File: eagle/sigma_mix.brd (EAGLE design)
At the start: 117.5 x 59.5 mm, 155 parts, among them J1 POWER_JACK, J2 RCA_JACK_CUI, J3 RCA_JACK_CUI, J4 RCA_JACK_CUI, J5 RCA_JACK_CUI, J6 RCA_JACK_X2_CUI, J7 RCA_JACK_X2_CUI, J8 RCA_JACK_X2_CUI, J9 RCA_JACK_X2_CUI, U1 MCP1726, U2 MCP73871, U3 ADM811TARTZ-REEL7, U4 ADAU1701JSTZ, U5 ADAU1701JSTZ, X1 2510-, X2 2510-, X3 12.288MHz, X4 12.288MHz

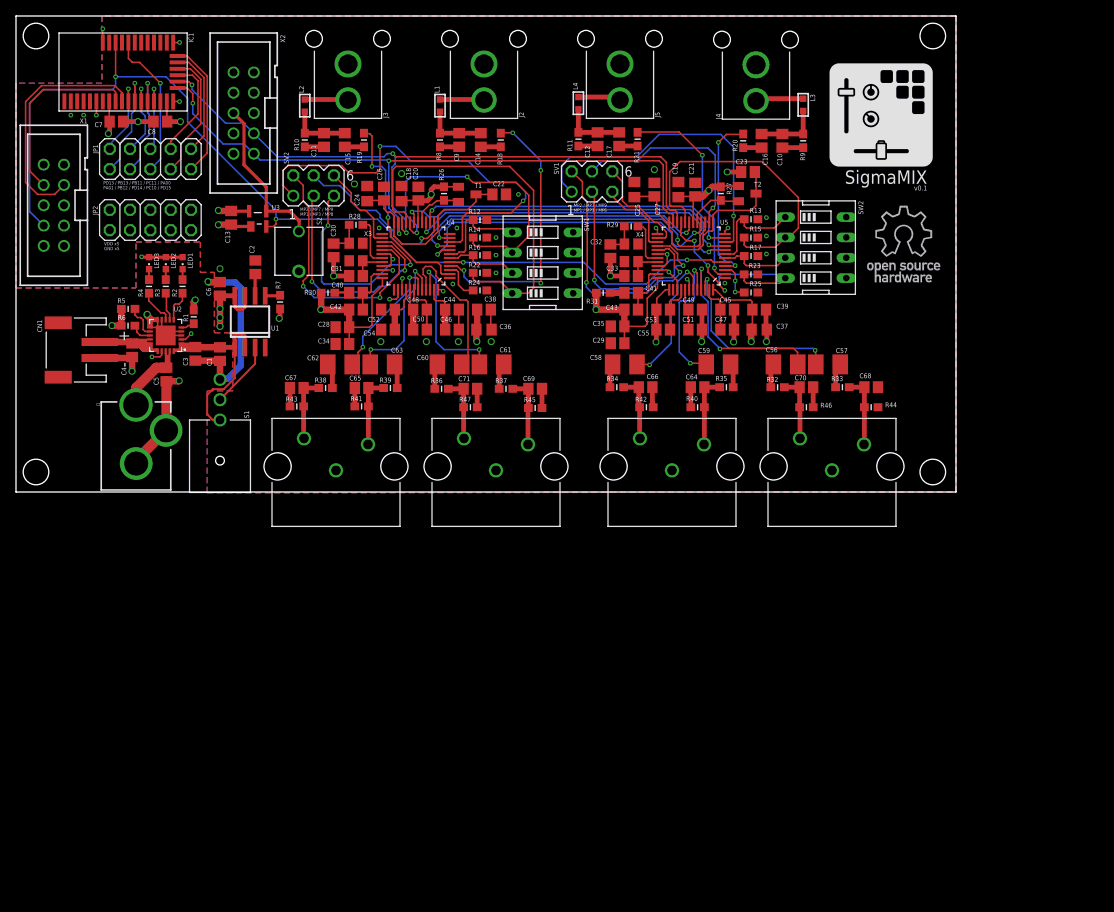
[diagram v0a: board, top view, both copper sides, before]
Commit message: Release ver0.2.
Fixed some bugs of issue.
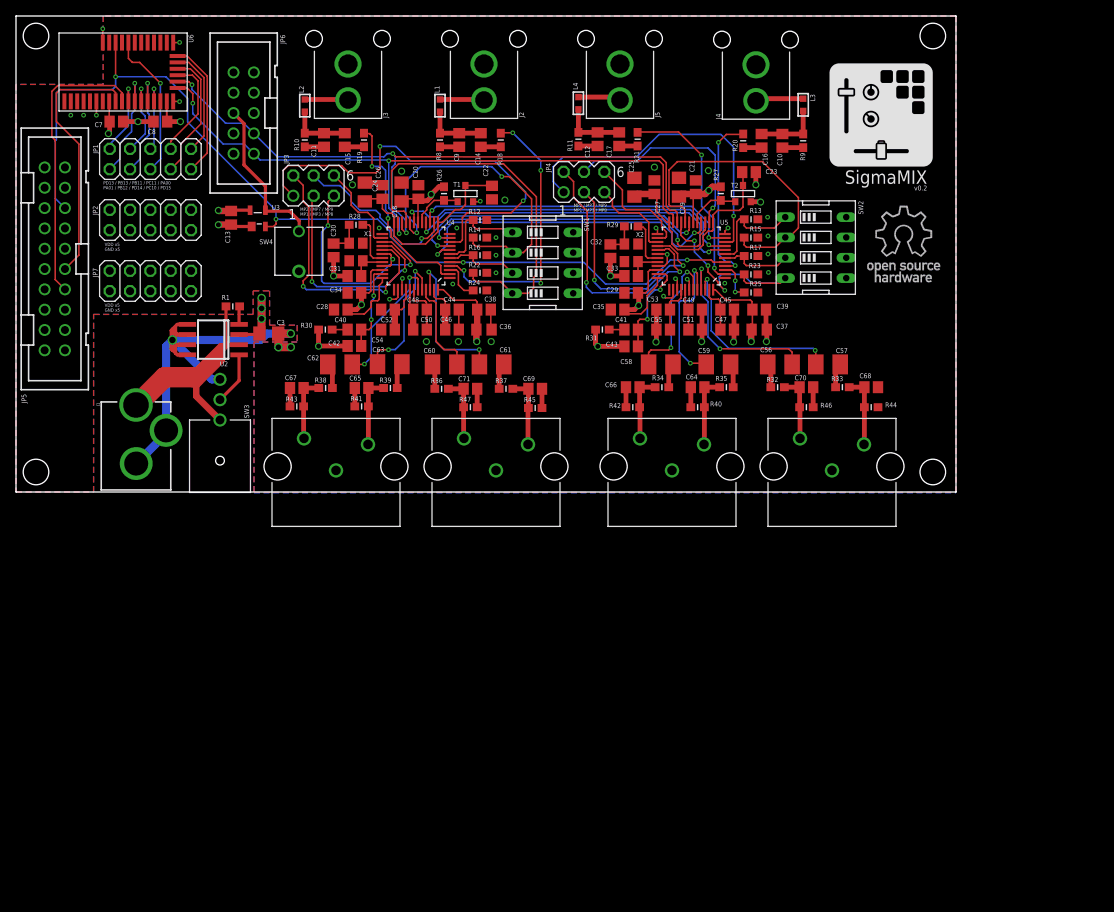
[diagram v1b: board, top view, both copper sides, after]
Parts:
- removed C1, C4, C5: 4.7uF, rcl:C2012
- removed C2: 1000pF, rcl:C2012
- removed C6: 1uF, rcl:C2012
- removed CN1: (no value), adafruit:JST-PH-2-SMT-RA
- removed LED1, LED2, LED3: (no value), led:CHIPLED_0603
- removed R2, R3, R4, R6: 1k, SparkFun:0603-RES
- removed R5: 10k, SparkFun:0603-RES
- removed R7: 100k, SparkFun:0603-RES
- removed SV1: (no value), con-lstb:MA03-2
- removed U1: MCP1726, tkrworks:SOIC8
- removed X3, X4: 12.288MHz, tkrworks2:ABMXX-XXMHZ-XX-X-X-X
- added JP4: (no value), con-lstb:MA03-2
- added JP5: SWD Interface, con-3m:PAK100/2500-20
- added JP6: USBi, con-3m:PAK100/2500-10
- added JP7: (no value), pinhead:2X05
- C18, C19, C24, C25: device rcl:C0805 -> rcl:R/2012-12R
- C3: value 4.7uF -> 10uF; device rcl:C2012 -> rcl:R/2012-12R
- C40, C41: value 0.1uF -> 56nF
- C42, C43: value 10uF -> 3.3nF
- R1: value 10k -> 100k
- T1, T2: device transistor:SOT23-EBC -> zetex:SOT-23
- U2: value MCP73871 -> (none); device tkrworks:QFN20 -> tkrworks:SOIC8
- U3: device ADI-Phase-2:SOT192P237X117-4N -> ADI-Phase-2:SOT143P290X130-4N
- X1, X2: value 2510- -> 12.288MHz; device con-3m:PAK100/2500-10 -> tkrworks2:ABMXX-XXMHZ-XX-X-X-X
- moved X2 51.5 mm to (53.6, 76.0), turned to 270 degrees
- moved X1 38.2 mm to (19.2, 76.1), turned to 270 degrees
- moved C3 9.52 mm to (8.30, 65.9), turned to 180 degrees
- moved C34 6.57 mm to (19.0, 71.0)
- moved C29 6.53 mm to (53.6, 71.0)
- moved U2 5.96 mm to (1.35, 65.2), turned to 90 degrees
- moved R34 5.64 mm to (57.4, 59.2), turned to 180 degrees
- moved R1 5.05 mm to (3.80, 69.3), turned to 0 degrees
- moved R30 4.61 mm to (15.4, 66.4)
- moved C40 4.60 mm to (19.0, 66.4)
- moved R31 4.60 mm to (50.0, 66.4)
- moved C43 4.60 mm to (53.6, 64.3)
- moved C41 4.60 mm to (53.6, 66.4)
- moved C42 4.55 mm to (19.0, 64.3)
- moved C58 4.50 mm to (57.3, 62.0), turned to 180 degrees
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- renumbered IC1 to U6, S1 to SW3, S2 to SW4, SV2 to JP3
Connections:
- removed net DEBUG_CLOCK: U6.P$9, X1.8
- removed net DEBUG_DATA: U6.P$10, X1.7
- removed net N$13: C2.1, U1.6
- removed net N$14: R7.1, U1.5
- removed net N$17: R2.2, U2.P$6
- removed net N$18: R3.2, U2.P$7
- removed net N$23: LED1.C, R2.1
- removed net N$25: LED2.C, R3.1
- removed net N$27: LED3.C, R4.1
- removed net N$29: R4.2, U2.P$8
- removed net N$30: R1.2, U2.P$5
- removed net N$31: R5.2, U2.P$12
- removed net N$32: R6.2, U2.P$13
- removed net N$5: C22.1, C24.1, C26.1, T1.C, U4.13, U4.24
- removed net VBAT: C4.1, CN1.1, U2.P$14, U2.P$15, U2.P$16
- removed net VBUS: C5.1, J1.PWR, LED1.A, LED2.A, LED3.A, U2.P$17, U2.P$18, U2.P$19, U2.P$2
- new net 5V-SUPPLY: JP5.19
- new net DVDD: C22.1, C24.+, C26.1, T1.1, U4.13, U4.24
- new net FLG: R1.2, U2.4
- new net SWCLK: JP5.9, U6.P$9
- new net SWDIO: JP5.7, U6.P$10
- new net SWO: JP5.13
- new net VTREF: JP5.1
- net *RESET: now also JP5.15; no longer X1.4
- net BRD_RESET: now also JP6.6; no longer X2.6
- net GND: now also C18.-, C19.-, C24.-, C25.-, C3.-, JP5.10, JP5.12, JP5.14, JP5.16, JP5.18, JP5.20, JP5.4, JP5.6, JP5.8, JP6.10, JP7.10, JP7.2, JP7.4, JP7.6, JP7.8, U2.5, U2.6, U2.7, U2.8; no longer C1.2, C18.2, C19.2, C2.2, C24.2, C25.2, C3.2, C4.2, C5.2, C6.2, CN1.2, R1.1, R5.1, R6.1, U1.4, U2.P$10, U2.P$11, U2.P$21, U2.P$3, U2.P$4, U2.P$9, X1.10, X2.10
- net MCLKI_1: now also X1.P$3; no longer X3.P$3
- net MCLKI_2: now also X2.P$3; no longer X4.P$3
- net MP1_2: now also JP4.1; no longer SV1.1
- net MP2_2: now also JP4.2; no longer SV1.2
- net MP3_2: now also JP4.3; no longer SV1.3
- net MP7_2: now also JP4.4; no longer SV1.4
- net MP8_2: now also JP4.5; no longer SV1.5
- net MP9_2: now also JP4.6; no longer SV1.6
- net N$1: now also T1.3; no longer T1.B
- net N$11: now also JP6.2; no longer X2.2
- net N$36: now also T2.3; no longer T2.B
- net N$37: now also C25.+, T2.1; no longer C25.1, T2.C
- net N$43: now also X2.P$1; no longer X4.P$1
- net N$9: now also X1.P$1; no longer X3.P$1
- net PSW: now also U2.1; no longer U1.3
- net SCL: now also JP6.1; no longer X2.1
- net SDA: now also JP6.3; no longer X2.3
- net VDD: now also C18.+, C19.+, C3.+, JP7.1, JP7.3, JP7.5, JP7.7, JP7.9, T1.2, T2.2, U2.3; no longer C18.1, C19.1, C6.1, R7.2, T1.E, T2.E, U1.7, U1.8, X1.9
- net VIN: now also J1.PWR, R1.1, U2.2; no longer C1.1, C3.1, U1.1, U1.2, U2.P$1, U2.P$20
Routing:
- net SWDIO: track 0.00 -> 35.9 mm
- net SWCLK: track 0.00 -> 32.7 mm
- net DEBUG_DATA: track 30.3 -> 0.00 mm
- net VBAT: track 26.1 -> 0.00 mm
- net DVDD: track 0.00 -> 25.7 mm
- net N$5: track 24.3 -> 0.00 mm
- net DEBUG_CLOCK: track 23.7 -> 0.00 mm
- net VBUS: track 22.3 -> 0.00 mm, vias 3 -> 0
- net VIN: track 35.2 -> 55.4 mm
- net VOUT1_1: track 19.0 -> 12.0 mm
- net N$39: track 6.62 -> 12.6 mm, vias 0 -> 2
- net *RESET: track 127.7 -> 122.9 mm
- net N$3: track 6.56 -> 11.3 mm, vias 0 -> 2
- net N$29: track 4.43 -> 0.00 mm
- net N$31: track 4.21 -> 0.00 mm
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- removed copper zone on layer 3, net VBUS
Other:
- board text added: "v0.2"
- board text removed: "v0.1"

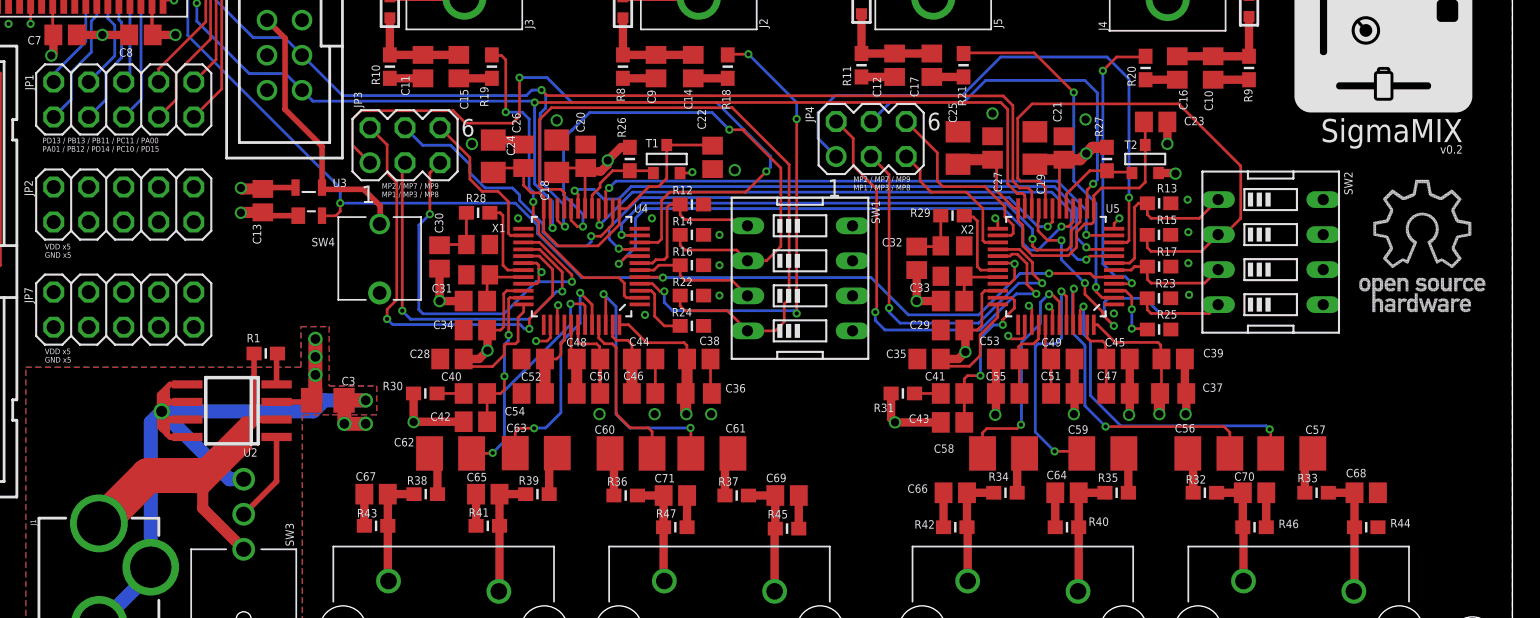
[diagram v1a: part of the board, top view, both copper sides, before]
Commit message: Release ver0.3.
Fixed the issue #11, #12, #13.
Fixed some silk positions.
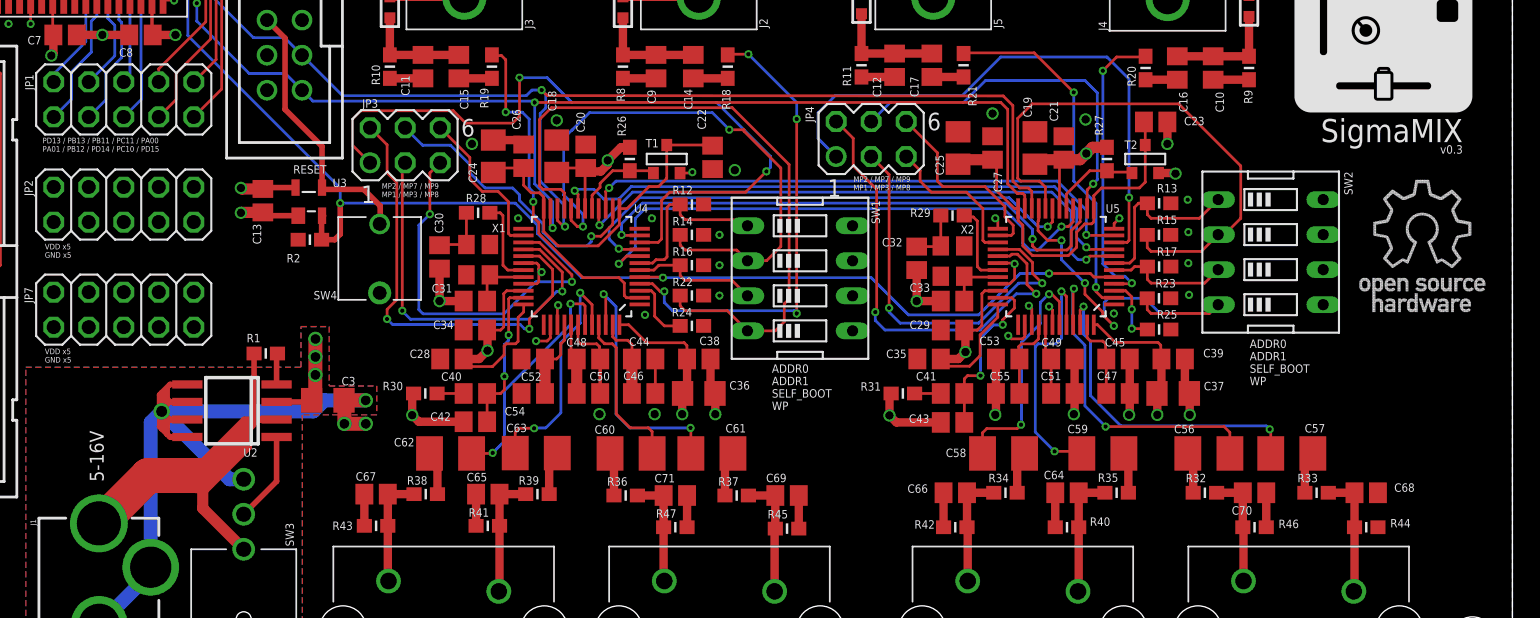
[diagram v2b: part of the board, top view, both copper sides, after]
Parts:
- added R2: 10k, SparkFun:0603-RES
- C36, C37: device rcl:C0805 -> rcl:R/2012-12R
- R18, R19, R20, R21: value 8k06 -> 8R06
- R32, R33, R34, R35, R36, R37, R38, R39: value 56k2 -> 56R2
- turned C36 to 180 degrees
- turned C37 to 180 degrees
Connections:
- net *RESET: now also R2.2
- net GND: now also C36.-, C37.-, R2.1; no longer C36.2, C37.2
- net VDD: now also C36.+, C37.+; no longer C36.1, C37.1
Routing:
- net *RESET: track 122.9 -> 126.5 mm
- net GND: track 159.8 -> 161.6 mm
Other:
- board text added: "5-16V"
- board text added: "ADDR0"
- board text added: "ADDR1"
- board text added: "RESET"
- board text added: "SELF_BOOT"
- board text added: "WP"
- board text added: "v0.3"
- board text removed: "v0.2"

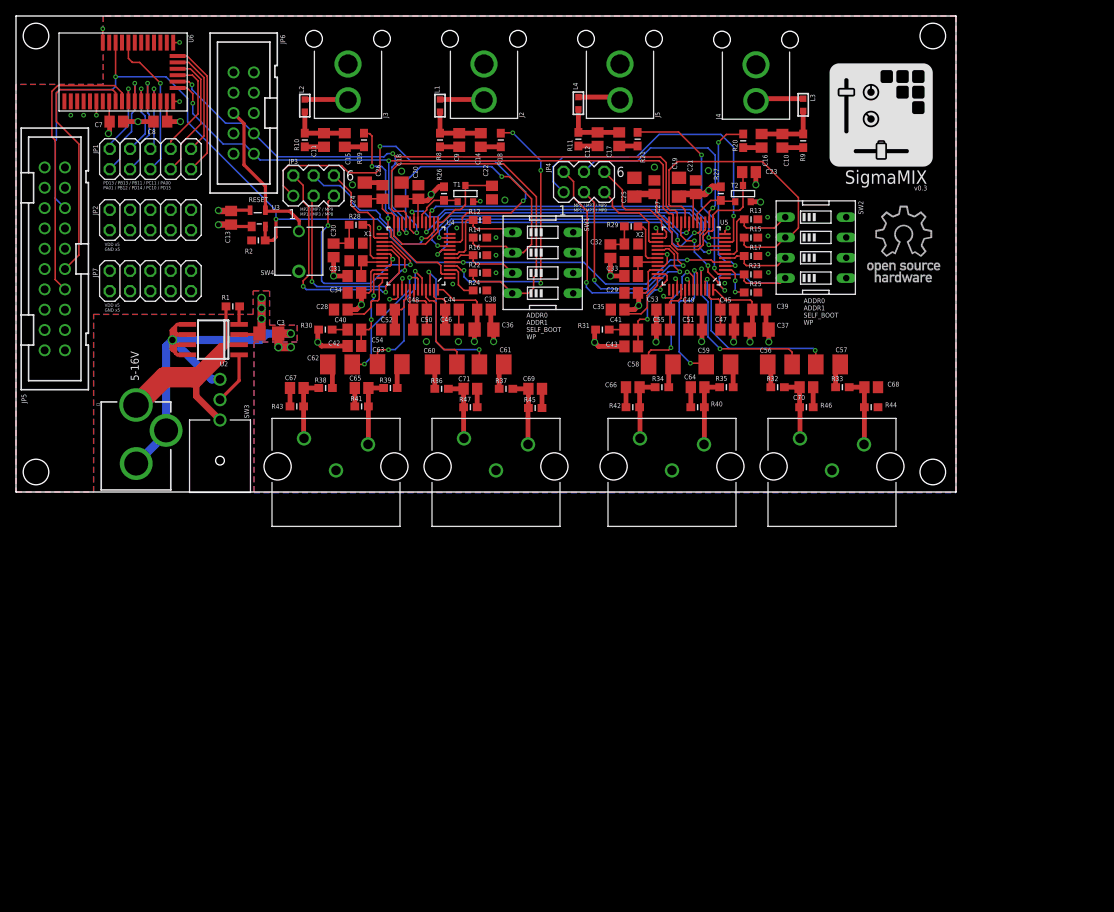
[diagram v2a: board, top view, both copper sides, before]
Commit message: Reseale ver 0.4.
Fxed the issues #14, #15, #16 and #18.
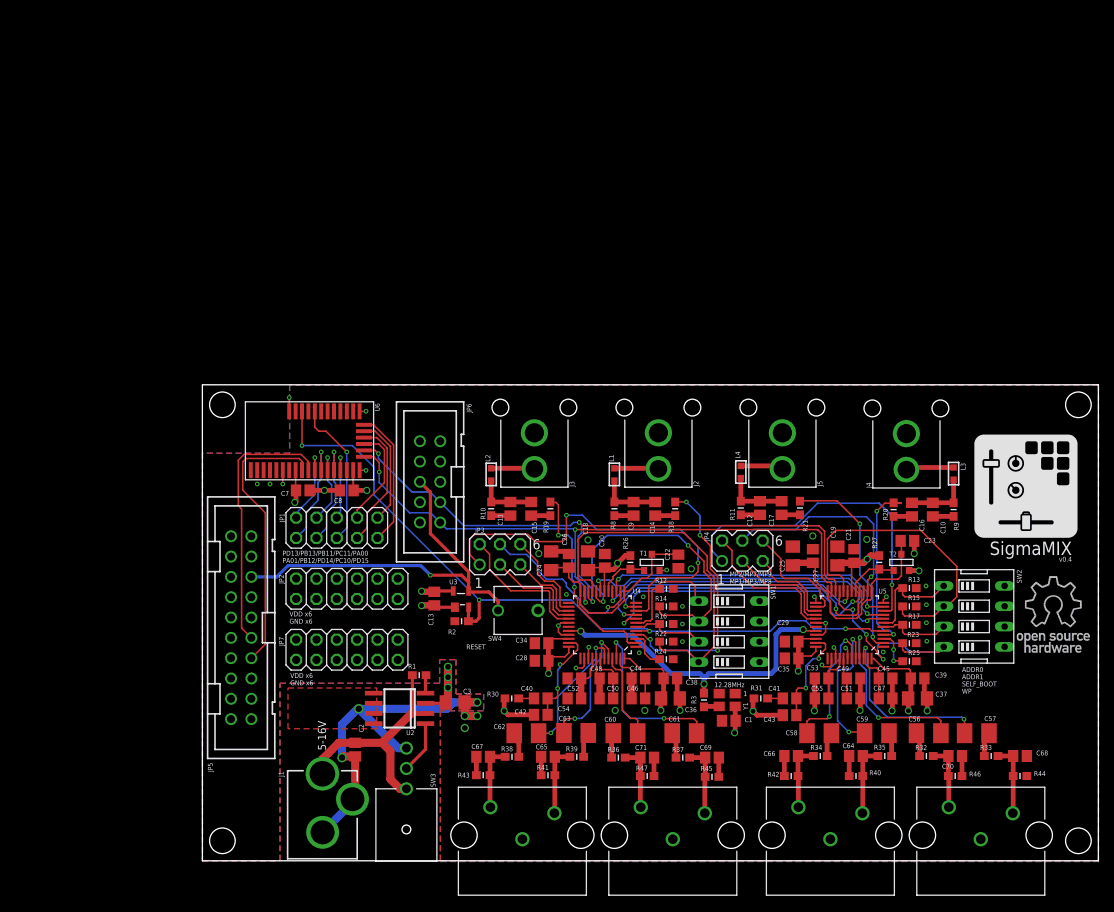
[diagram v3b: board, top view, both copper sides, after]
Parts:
- removed C30, C31, C32, C33: 22pF, rcl:C2012
- removed R28, R29: 100, SparkFun:0603-RES
- removed X1, X2: 12.288MHz, tkrworks2:ABMXX-XXMHZ-XX-X-X-X
- added C1: 0.1uF, rcl:C2012
- added C2: 1uF, rcl:C2012
- added R3: 0, SparkFun:0603-RES
- added Y1: 12.28MHz, tkrworks2:SG-210
- JP2, JP7: device pinhead:2X05 -> pinhead:2X06
- moved U3 54.0 mm to (32.3, 32.7)
- moved C13 54.0 mm to (29.0, 32.8)
- moved R2 54.0 mm to (32.4, 29.9)
- moved SW4 52.6 mm to (39.5, 31.3), turned to 180 degrees
- moved JP7 52.2 mm to (18.1, 26.4)
- moved JP2 52.2 mm to (18.1, 34.0)
- moved C61 52.0 mm to (60.2, 15.9), turned to 0 degrees
- moved C3 51.7 mm to (31.6, 19.8)
- moved C36 51.7 mm to (58.5, 20.3)
- moved C38 51.7 mm to (58.5, 22.8)
- moved C40 51.7 mm to (42.3, 20.3)
- moved C44 51.7 mm to (54.5, 22.8)
- moved C46 51.7 mm to (54.5, 20.3)
- moved C48 51.7 mm to (50.5, 22.8)
- moved C50 51.7 mm to (50.5, 20.3)
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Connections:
- removed net MCLKI_1: C31.1, U4.32, X1.P$3
- removed net MCLKI_2: C33.1, U5.32, X2.P$3
- removed net N$43: C32.1, R29.1, X2.P$1
- removed net N$9: C30.1, R28.1, X1.P$1
- removed net OSCO_1: R28.2, U4.31
- removed net OSCO_2: R29.2, U5.31
- removed net VTREF: JP5.1
- new net MCLKI: R3.2, U4.32, U5.32
- new net N$5: R3.1, Y1.P$3
- net *RESET: no longer JP5.15
- net BRD_RESET: now also JP5.15
- net GND: now also C1.2, C2.2, JP2.12, JP7.12, Y1.P$2; no longer C30.2, C31.2, C32.2, C33.2
- net SWCLK: now also JP5.7; no longer JP5.9
- net SWDIO: now also JP5.9; no longer JP5.7
- net VDD: now also C1.1, JP2.11, JP5.1, JP7.11, Y1.P$4
- net VIN: now also C2.1
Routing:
- net MCLKI: track 0.00 -> 40.3 mm, vias 0 -> 3
- net BRD_RESET: track 19.9 -> 50.1 mm, vias 0 -> 1
- net *RESET: track 126.5 -> 97.0 mm
- net VIN: track 55.4 -> 29.4 mm
- net GND: track 161.6 -> 136.1 mm
- net MP8_1: track 28.5 -> 9.78 mm, vias 2 -> 0
- net MP3_1: track 28.4 -> 12.6 mm, vias 2 -> 0
- net MP3_2: track 29.1 -> 13.4 mm, vias 2 -> 0
- net MP2_1: track 33.1 -> 17.5 mm, vias 2 -> 0
- net MP2_2: track 33.7 -> 18.3 mm, vias 2 -> 0
- net VDD: track 109.9 -> 100.4 mm, vias 18 -> 19
- net OSCO_1: track 6.26 -> 0.00 mm
- net OSCO_2: track 6.00 -> 0.00 mm
- net MCLKI_1: track 4.48 -> 0.00 mm
- net N$9: track 4.27 -> 0.00 mm
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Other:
- board size 117.5 x 59.5 mm -> 112 x 59.5 mm
- board text added: "MP2/MP7/MP9 MP1/MP3/MP8"
- board text added: "PD13/PB13/PB11/PC11/PA00 PA01/PB12/PD14/PC10/PD15"
- board text added: "VDD x6 GND x6"
- board text added: "v0.4"
- board text removed: "MP2 / MP7 / MP9 MP1 / MP3 / MP8"
- board text removed: "PD13 / PB13 / PB11 / PC11 / PA00 PA01 / PB12 / PD14 / PC10 / PD15"
- board text removed: "VDD x5 GND x5"
- board text removed: "v0.3"
